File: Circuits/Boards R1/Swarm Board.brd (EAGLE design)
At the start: 63.5 x 63.5 mm, 93 parts, among them CON1 ISP(2X3), T1 NPN2N2222, T10 TEFT4300, T11 NPN2N2222, T13 NPN2N2222, T14 NPN2N2222, T15 NPN2N2222, T16 NPN2N2222, T17 NPN2N2222, T18 NPN2N2222, T2 NPN2N2222, T3 NPN2N2222, T4 TEFT4300, T5 TEFT4300, T6 TEFT4300, T7 TEFT4300, T8 TEFT4300, T9 TEFT4300, U1 ATMEGA324P, U3 TB6552FN/FNG

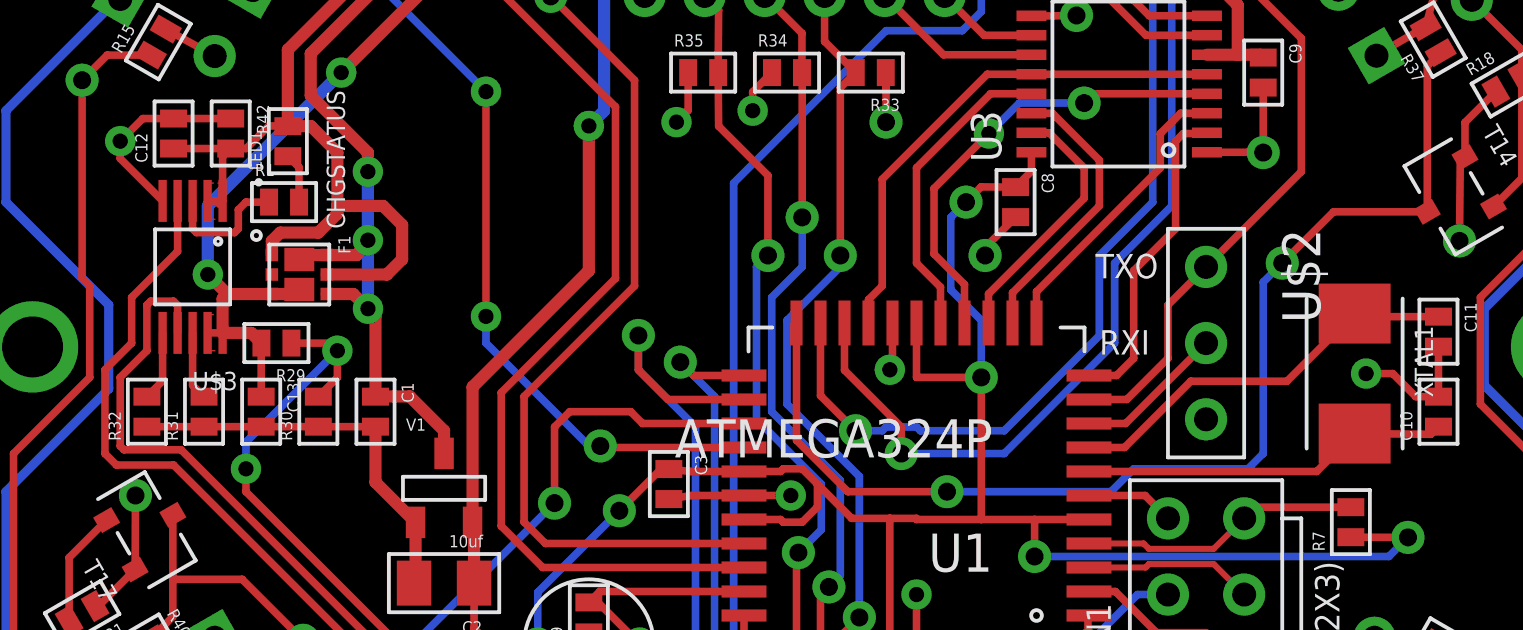
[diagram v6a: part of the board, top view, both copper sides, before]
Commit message: 
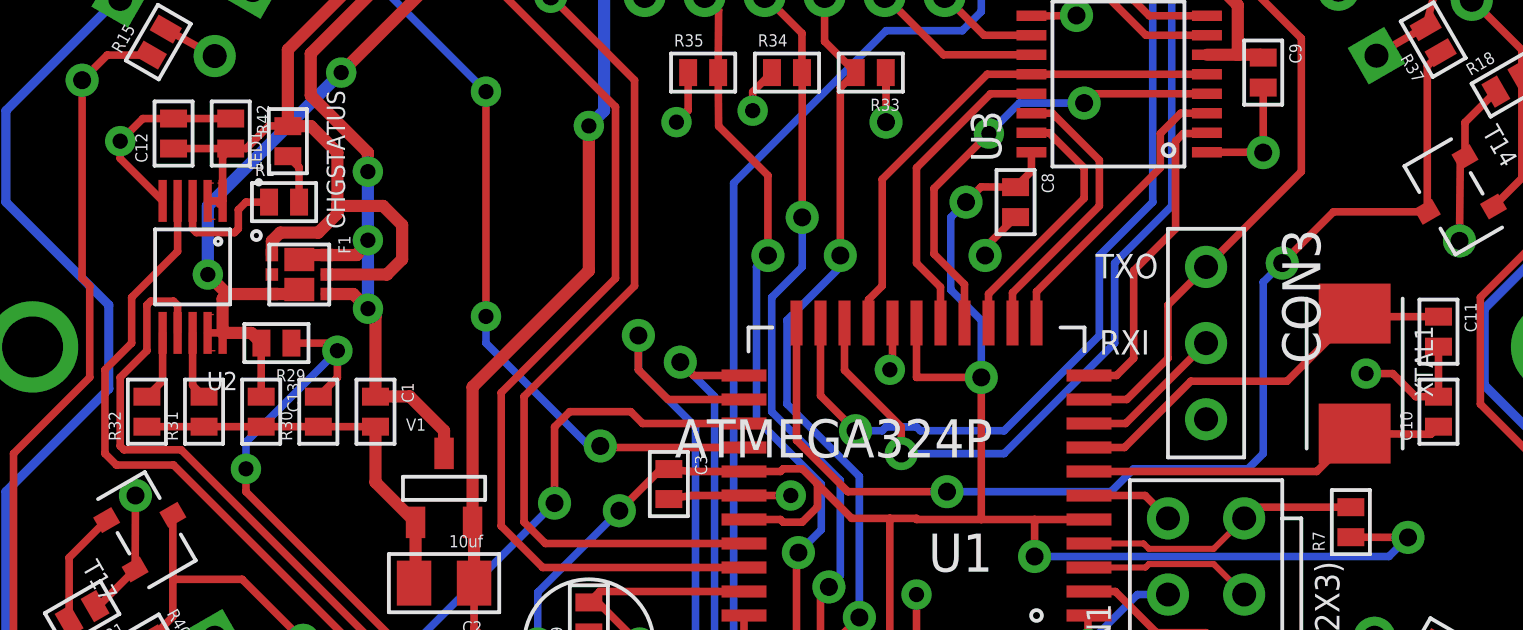
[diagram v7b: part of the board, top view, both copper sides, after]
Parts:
- renumbered U$1 to CON2, U$2 to CON3, U$3 to U2
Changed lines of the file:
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@@
 <element name="R26" library="Passive" package="0603" value="750" x="31.75" y="14.605"/>
 <element name="R28" library="Passive" package="0603" value="1k" x="40.259" y="15.113"/>
-<element name="U$1" library="Mechanical" package="FEMALE_HEADER_2MM_2X6" value="MAIN_CONNECTOR" x="31.75" y="44.45" rot="MR0"/>
-<element name="U$2" library="Mechanical" package="3PINHEADER_.100&quot;" value="FTDI_3PIN" x="45.466" y="31.877" rot="R270"/>
+<element name="CON2" library="Mechanical" package="FEMALE_HEADER_2MM_2X6" value="MAIN_CONNECTOR" x="31.75" y="44.45" rot="MR0"/>
+<element name="CON3" library="Mechanical" package="3PINHEADER_.100&quot;" value="FTDI_3PIN" x="45.466" y="31.877" rot="R270"/>
 <element name="T10" library="Passive" package="3MM_LED_RA" value="TEFT4300" x="27.94" y="57.15"/>
 <element name="R27" library="Passive" package="0603" value="" x="30.734" y="55.499" rot="R270"/>
@@
 <element name="R40" library="Passive" package="0603" value="" x="10.541" y="21.59" rot="R300"/>
 <element name="R41" library="Passive" package="0603" value="" x="12.319" y="45.085" rot="R240"/>
-<element name="U$3" library="PowerIC" package="MSOP10" value="MCP73833" x="11.684" y="34.417" rot="R180"/>
+<element name="U2" library="PowerIC" package="MSOP10" value="MCP73833" x="11.684" y="34.417" rot="R180"/>
 <element name="R29" library="Passive" package="0603" value="7k" x="14.478" y="31.877" rot="R180"/>
 <element name="R30" library="Passive" package="0603" value="18k" x="15.875" y="29.591" rot="R90"/>
@@
 <wire x1="24.368" y1="59.69" x2="24.511" y2="59.309" width="0.3048" layer="1"/>
 <wire x1="24.511" y1="59.309" x2="26.67" y2="57.15" width="0.3048" layer="1"/>
-<contactref element="U$1" pad="8"/>
+<contactref element="CON2" pad="8"/>
 <wire x1="41.564" y1="25.997" x2="39.751" y2="25.997" width="0.254" layer="1"/>
 <via x="37.973" y="30.734" extent="1-16" drill="0.6" diameter="0.4064"/>
@@
 <contactref element="C2" pad="2"/>
 <contactref element="CON1" pad="3"/>
-<contactref element="U$2" pad="3"/>
+<contactref element="CON3" pad="3"/>
 <contactref element="T1" pad="2"/>
 <contactref element="R9" pad="1"/>
@@
 <contactref element="U3" pad="9"/>
 <contactref element="C9" pad="2"/>
-<contactref element="U$1" pad="6"/>
+<contactref element="CON2" pad="6"/>
 <contactref element="ANT3" pad="P$1"/>
 <contactref element="R27" pad="1"/>
@@
 <via x="20.447" y="59.69" extent="1-16" drill="0.6" diameter="0.4064"/>
 <wire x1="22.368" y1="59.69" x2="22.037" y2="59.259" width="0.254" layer="1"/>
-<contactref element="U$1" pad="9"/>
+<contactref element="CON2" pad="9"/>
 <wire x1="34.798" y1="40.378" x2="34.798" y2="39.243" width="0.254" layer="1"/>
 <via x="34.798" y="39.243" extent="1-16" drill="0.6" diameter="0.4064"/>
 <wire x1="25.765" y1="8.316" x2="26.728" y2="8.316" width="0.254" layer="1"/>
 <wire x1="26.728" y1="8.316" x2="27.686" y2="7.358" width="0.254" layer="1"/>
-<contactref element="U$3" pad="5"/>
+<contactref element="U2" pad="5"/>
 <contactref element="R30" pad="1"/>
 <contactref element="C13" pad="2"/>
@@
 </signal>
 <signal name="+VBAT">
-<contactref element="U$1" pad="7"/>
+<contactref element="CON2" pad="7"/>
 <wire x1="21.209" y1="45.45" x2="26.75" y2="45.45" width="0.4064" layer="1"/>
 <contactref element="R29" pad="2"/>
@@
 <contactref element="F1" pad="8"/>
 <contactref element="F1" pad="3"/>
-<contactref element="U$3" pad="10"/>
-<contactref element="U$3" pad="9"/>
+<contactref element="U2" pad="10"/>
+<contactref element="U2" pad="9"/>
 <wire x1="12.184" y1="32.217" x2="12.684" y2="32.217" width="0.254" layer="1"/>
 <wire x1="12.684" y1="32.217" x2="13.638" y2="32.217" width="0.4064" layer="1"/>
@@
 <contactref element="ANT1" pad="P$1"/>
 <wire x1="24.003" y1="50.8" x2="31.75" y2="50.8" width="0.4064" layer="1"/>
-<contactref element="U$3" pad="2"/>
-<contactref element="U$3" pad="1"/>
+<contactref element="U2" pad="2"/>
+<contactref element="U2" pad="1"/>
 <contactref element="C12" pad="1"/>
 <contactref element="F1" pad="1"/>
@@
 </signal>
 <signal name="CHGDETECT">
-<contactref element="U$3" pad="7"/>
+<contactref element="U2" pad="7"/>
 <wire x1="11.184" y1="32.217" x2="11.184" y2="33.139" width="0.254" layer="1"/>
 <wire x1="11.184" y1="33.139" x2="11.049" y2="33.274" width="0.254" layer="1"/>
@@
 <contactref element="R33" pad="2"/>
 <contactref element="U1" pad="36"/>
-<contactref element="U$1" pad="3"/>
+<contactref element="CON2" pad="3"/>
 <wire x1="33.414" y1="21.047" x2="33.414" y2="22.238" width="0.254" layer="1"/>
 <wire x1="33.414" y1="22.238" x2="33.909" y2="22.733" width="0.254" layer="1"/>
@@
 <contactref element="R34" pad="2"/>
 <contactref element="U1" pad="35"/>
-<contactref element="U$1" pad="4"/>
+<contactref element="CON2" pad="4"/>
 <wire x1="32.614" y1="21.047" x2="32.614" y2="23.47" width="0.254" layer="1"/>
 <wire x1="32.614" y1="23.47" x2="32.893" y2="23.749" width="0.254" layer="1"/>
@@
 <signal name="DATAANTENNA">
 <contactref element="U1" pad="10"/>
-<contactref element="U$2" pad="1"/>
+<contactref element="CON3" pad="1"/>
 <contactref element="ANT2" pad="P$1"/>
 <wire x1="41.564" y1="29.997" x2="42.824" y2="29.997" width="0.254" layer="1"/>
@@
 <signal name="N$8">
 <contactref element="U1" pad="9"/>
-<contactref element="U$2" pad="2"/>
+<contactref element="CON3" pad="2"/>
 <wire x1="41.564" y1="29.197" x2="42.786" y2="29.197" width="0.254" layer="1"/>
 <wire x1="42.786" y1="29.197" x2="45.466" y2="31.877" width="0.254" layer="1"/>
@@
 <signal name="MA+">
 <contactref element="U3" pad="7"/>
-<contactref element="U$1" pad="12"/>
+<contactref element="CON2" pad="12"/>
 <wire x1="45.495" y1="42.138" x2="43.46" y2="42.138" width="0.254" layer="1"/>
 <wire x1="43.46" y1="42.138" x2="40.132" y2="45.466" width="0.254" layer="1"/>
@@
 <signal name="MA-">
 <contactref element="U3" pad="8"/>
-<contactref element="U$1" pad="11"/>
+<contactref element="CON2" pad="11"/>
 <wire x1="45.495" y1="42.788" x2="43.572" y2="42.788" width="0.254" layer="1"/>
 <wire x1="43.572" y1="42.788" x2="39.751" y2="46.609" width="0.254" layer="1"/>
@@
 <signal name="MB+">
 <contactref element="U3" pad="11"/>
-<contactref element="U$1" pad="2"/>
+<contactref element="CON2" pad="2"/>
 <wire x1="39.645" y1="41.488" x2="36.712" y2="41.488" width="0.254" layer="1"/>
 <wire x1="36.712" y1="41.488" x2="34.75" y2="43.45" width="0.254" layer="1"/>
@@
 <signal name="MB-">
 <contactref element="U3" pad="10"/>
-<contactref element="U$1" pad="1"/>
+<contactref element="CON2" pad="1"/>
 <wire x1="39.645" y1="42.138" x2="38.062" y2="42.138" width="0.254" layer="1"/>
 <wire x1="38.062" y1="42.138" x2="36.75" y2="43.45" width="0.254" layer="1"/>
@@
 </signal>
 <signal name="CHGSTATUS">
-<contactref element="U$3" pad="4"/>
+<contactref element="U2" pad="4"/>
 <wire x1="11.184" y1="36.617" x2="11.184" y2="34.933" width="0.254" layer="1"/>
 <wire x1="11.184" y1="34.933" x2="9.652" y2="33.401" width="0.254" layer="1"/>
@@
 <contactref element="R35" pad="2"/>
 <contactref element="U1" pad="34"/>
-<contactref element="U$1" pad="5"/>
+<contactref element="CON2" pad="5"/>
 <wire x1="31.814" y1="21.047" x2="31.814" y2="24.829" width="0.254" layer="1"/>
 <wire x1="31.814" y1="24.829" x2="31.877" y2="24.892" width="0.254" layer="1"/>
@@
 </signal>
 <signal name="N$28">
-<contactref element="U$3" pad="6"/>
+<contactref element="U2" pad="6"/>
 <contactref element="R32" pad="2"/>
 <wire x1="10.684" y1="32.217" x2="10.684" y2="30.615" width="0.254" layer="1"/>
@@
 </signal>
 <signal name="N$33">
-<contactref element="U$3" pad="3"/>
+<contactref element="U2" pad="3"/>
 <contactref element="R1" pad="1"/>
 <wire x1="11.684" y1="36.617" x2="11.684" y2="35.687" width="0.254" layer="1"/>
@@
 </signal>
 <signal name="N$22">
-<contactref element="U$3" pad="8"/>
+<contactref element="U2" pad="8"/>
 <contactref element="R31" pad="2"/>
 <wire x1="11.684" y1="32.217" x2="11.684" y2="30.472" width="0.254" layer="1"/>
@@
 </signal>
 <signal name="N$7">
-<contactref element="U$1" pad="10"/>
+<contactref element="CON2" pad="10"/>
 <contactref element="T11" pad="3"/>
 <wire x1="35.052" y1="47.514" x2="34.782" y2="47.498" width="0.254" layer="1"/>

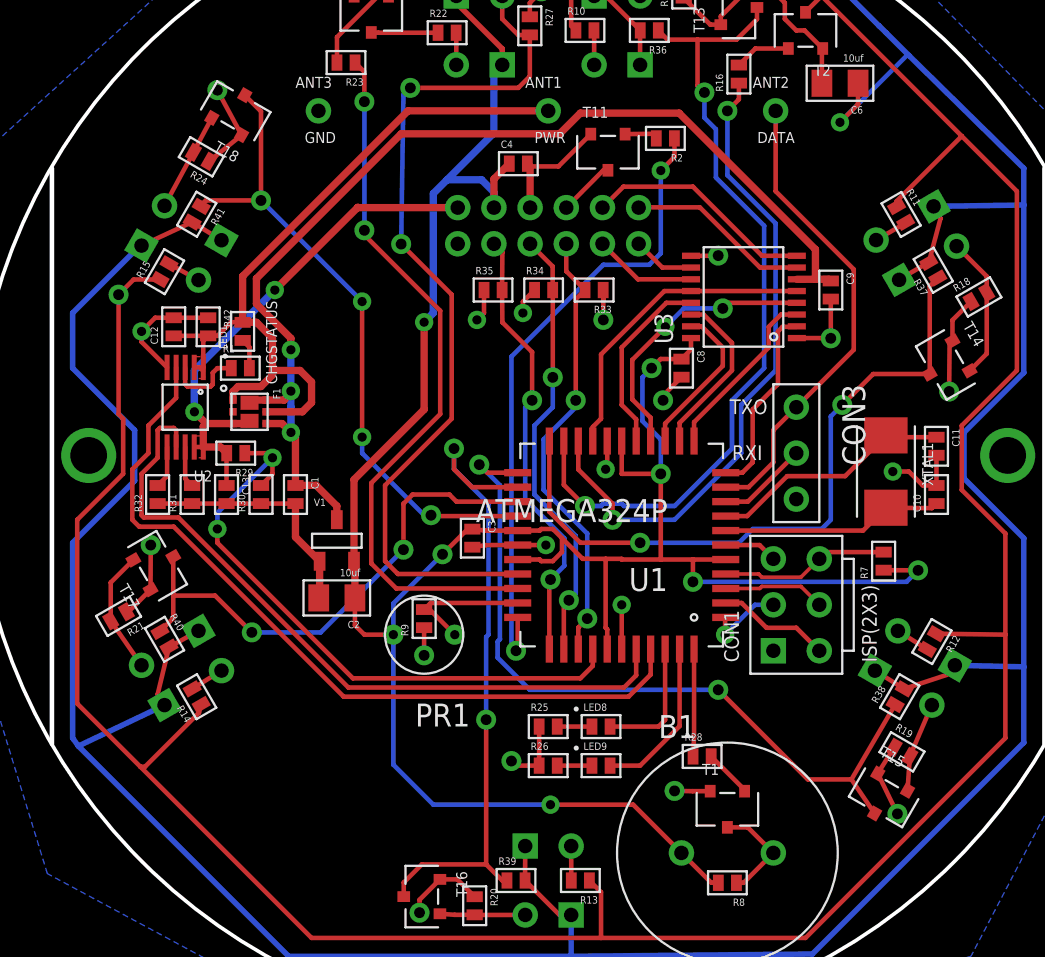
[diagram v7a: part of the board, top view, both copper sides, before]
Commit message: 
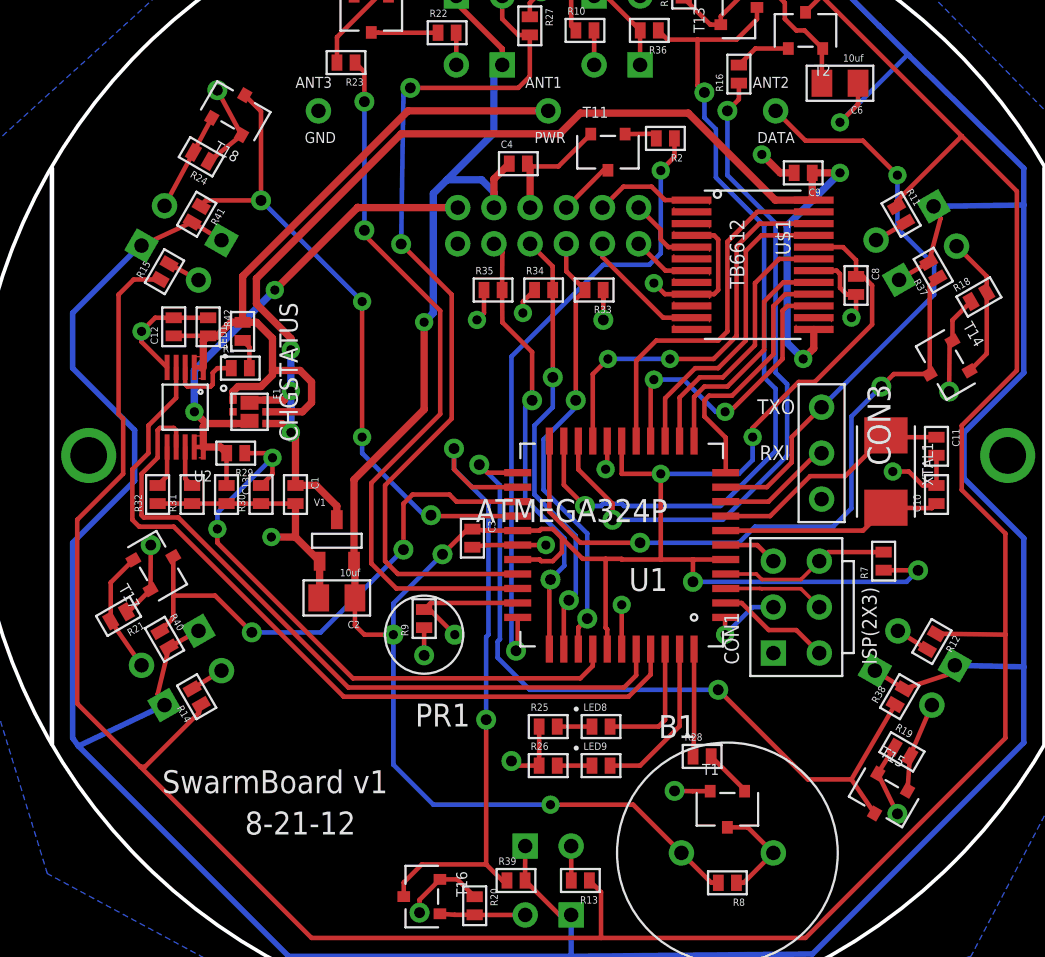
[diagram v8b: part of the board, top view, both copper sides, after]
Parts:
- removed U3: TB6552FN/FNG, DigitalIC:16SSOP
- added U$1: TB6612, DigitalIC:24SSOP
- moved C8 10.7 mm to (48.8, 41.1)
- moved C9 6.65 mm to (45.8, 47.4), turned to 180 degrees
- moved CON3 1.40 mm to (46.9, 31.9)
- moved CON1 0.13 mm to (45.5, 23.4)
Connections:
- net +3V: now also U$1.20; no longer U3.16
- net +VRAW: now also U$1.13, U$1.14, U$1.24; no longer U3.6
- net AIN1: now also U$1.21, U1.14; no longer U1.11, U3.2
- net AIN2: now also U$1.22, U1.19; no longer U1.12, U3.3
- net APWM: now also U$1.23, U1.16; no longer U1.15, U3.4
- net BIN1: now also U$1.17, U1.12; no longer U1.14, U3.15
- net BIN2: now also U$1.16, U1.11; no longer U1.13, U3.14
- net BPWM: now also U$1.15, U1.15; no longer U1.16, U3.13
- net GND: now also U$1.10, U$1.18, U$1.3, U$1.4, U$1.9; no longer U3.1, U3.9
- net MA+: now also CON2.11, U$1.1, U$1.2; no longer CON2.12, U3.7
- net MA-: now also CON2.12, U$1.5, U$1.6; no longer CON2.11, U3.8
- net MB+: now also U$1.11, U$1.12; no longer U3.11
- net MB-: now also U$1.7, U$1.8; no longer U3.10
- net STBY: now also U$1.19, U1.13; no longer U1.19, U3.12, U3.5
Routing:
- net +3V: track 368.9 -> 382.0 mm
- net AIN2: track 9.86 -> 22.3 mm, vias 0 -> 2
- net +VRAW: track 61.4 -> 73.4 mm, vias 3 -> 5
- net GND: track 106.0 -> 115.6 mm, vias 22 -> 23
- net MA-: track 12.8 -> 4.15 mm
- net BPWM: track 10.4 -> 17.0 mm, vias 0 -> 2
- net AIN1: track 10.7 -> 17.2 mm
- net DATAANTENNA: track 26.3 -> 32.4 mm, vias 0 -> 1
- net APWM: track 15.3 -> 20.6 mm, vias 2 -> 0
- net BIN2: track 9.54 -> 14.5 mm
- net BIN1: track 8.73 -> 13.2 mm
- net MA+: track 10.1 -> 5.71 mm
- net STBY: track 17.3 -> 15.0 mm
- net TRANSMITLEDS: track 36.4 -> 38.5 mm
- net RX1: track 45.3 -> 47.3 mm
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- added copper zone on layer 1, net +VRAW
- added copper zone on layer 1, net GND
- added copper zone on layer 1, net MA+
- added copper zone on layer 1, net MA-
- added copper zone on layer 1, net MB+
- added copper zone on layer 1, net MB-
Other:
- board text added: "8-21-12"
- board text added: "SwarmBoard v1"
